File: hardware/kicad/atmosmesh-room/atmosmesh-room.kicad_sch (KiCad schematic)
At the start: 38 parts, among them U1 IDEASPARK_ESP32_1V14_TFT_30PIN

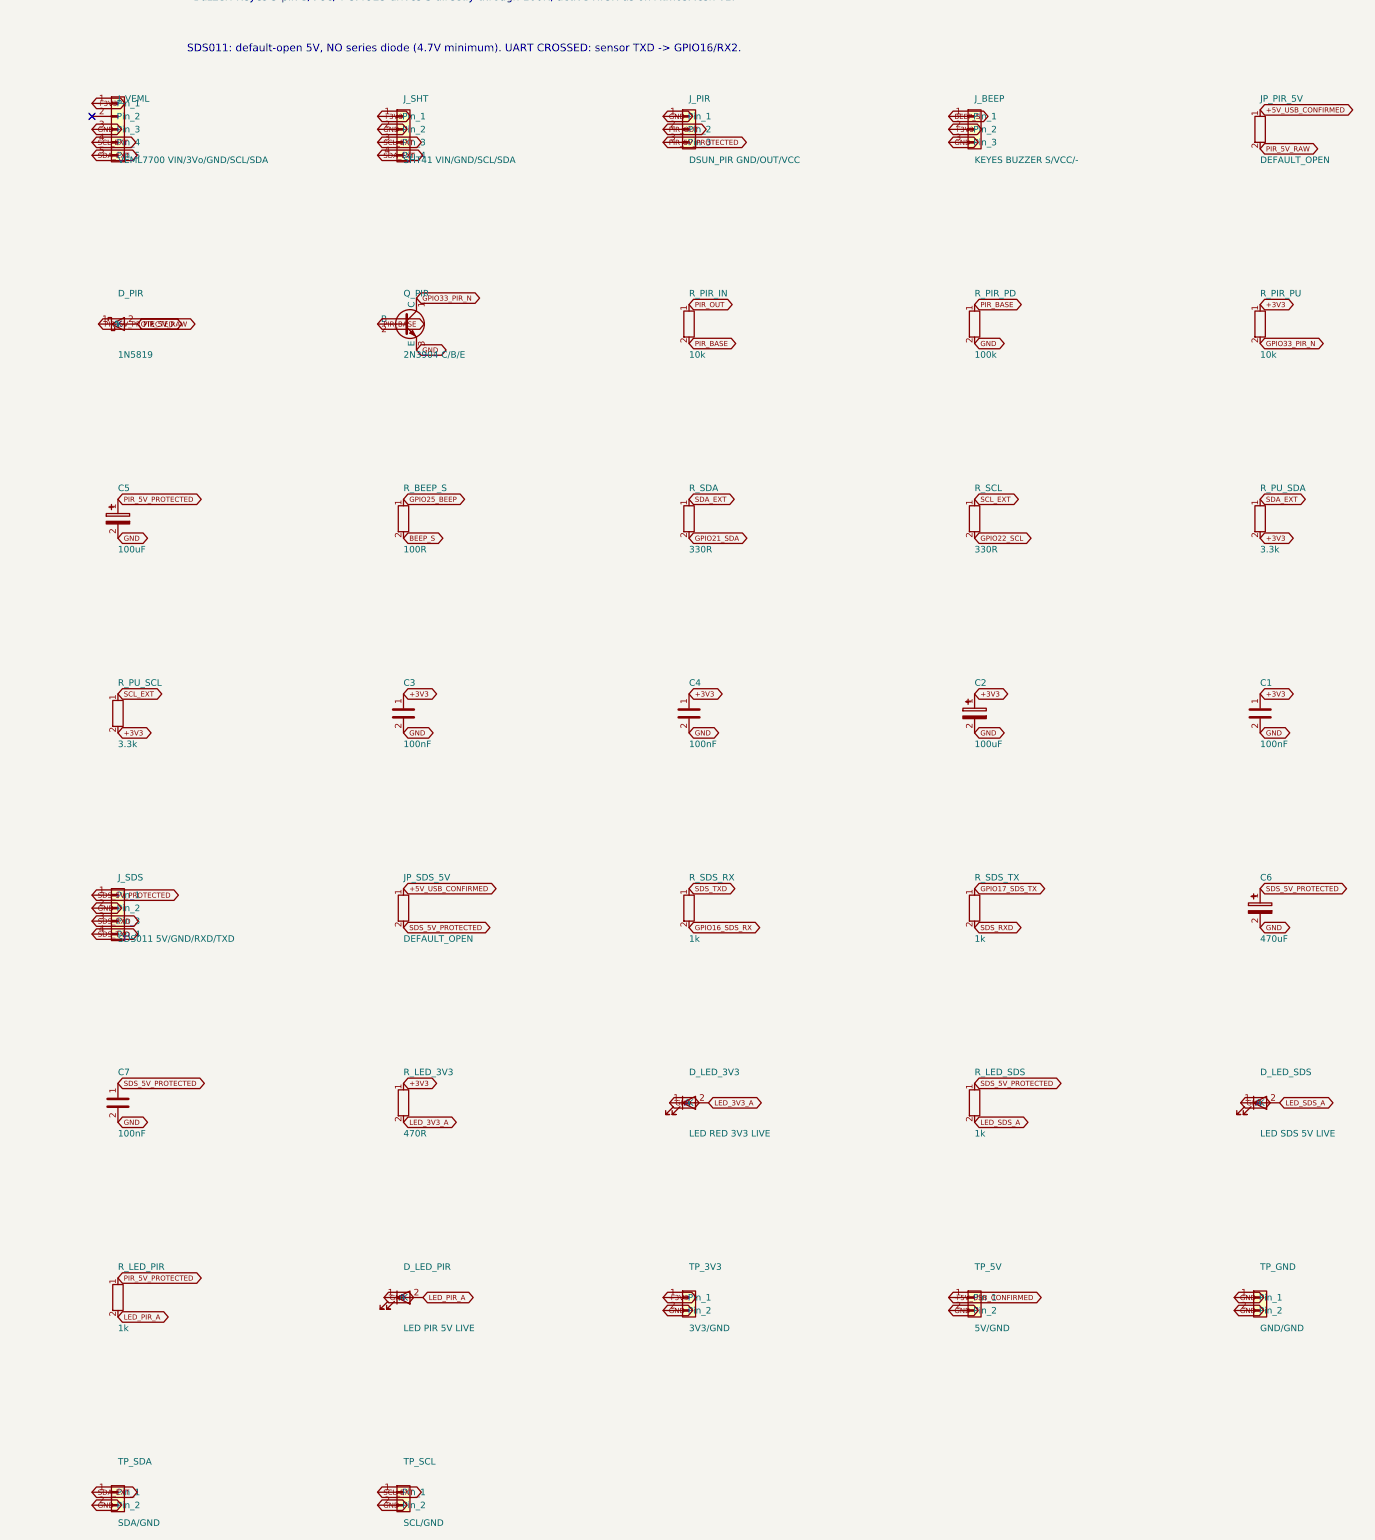
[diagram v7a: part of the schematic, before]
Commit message: :sparkles: feat(room): let the 5 V domain come from the bench supply instead of USB
The operator has a lab supply with adjustable voltage and current limit. That
changes the board, not just the procedure.

JP_5V_SRC is a 3-pin select feeding a new +5V_DOMAIN rail: shunt on 1-2 takes
the board's VIN, on 2-3 takes +5V_EXT from J_5V_EXT. JP_PIR_5V and JP_SDS_5V now
feed from +5V_DOMAIN rather than straight off VIN.

A 3-pin header accepts exactly one 2-pin shunt, so the two sources cannot be
bridged. Two independent 2-pin jumpers could both be closed and push the bench
supply back into the host's USB port. The generator refuses that arrangement and
refuses a domain wired straight to VIN; both mutation-proved.

This resolves an open blocker rather than measuring around it. spec-comparison.md
puts the USB rail near 650 mA peak coincidence before the SDS011 fan is added and
says 700 mA is not comfortable. With the external source selected the fan is not
on that rail at all.

Bring-up rule recorded in D-031: first power-up uses the external supply with the
current limit set just above the expected draw. A current-limited supply turns a
wiring error from a destroyed part into a supply that refuses to deliver - the
cheapest protection available to a project that has already lost an LDO once.

Also fixes a latent generator bug found on the way: silkscreen-vs-drawing layer
was chosen by a hard-coded index set, so every text inserted above position 8
silently moved a different label onto silkscreen. Layer is now stated per entry.

Gates: ERC 0, DRC 0 violations and 0 parity problems, both validators PASS,
git diff --check clean.
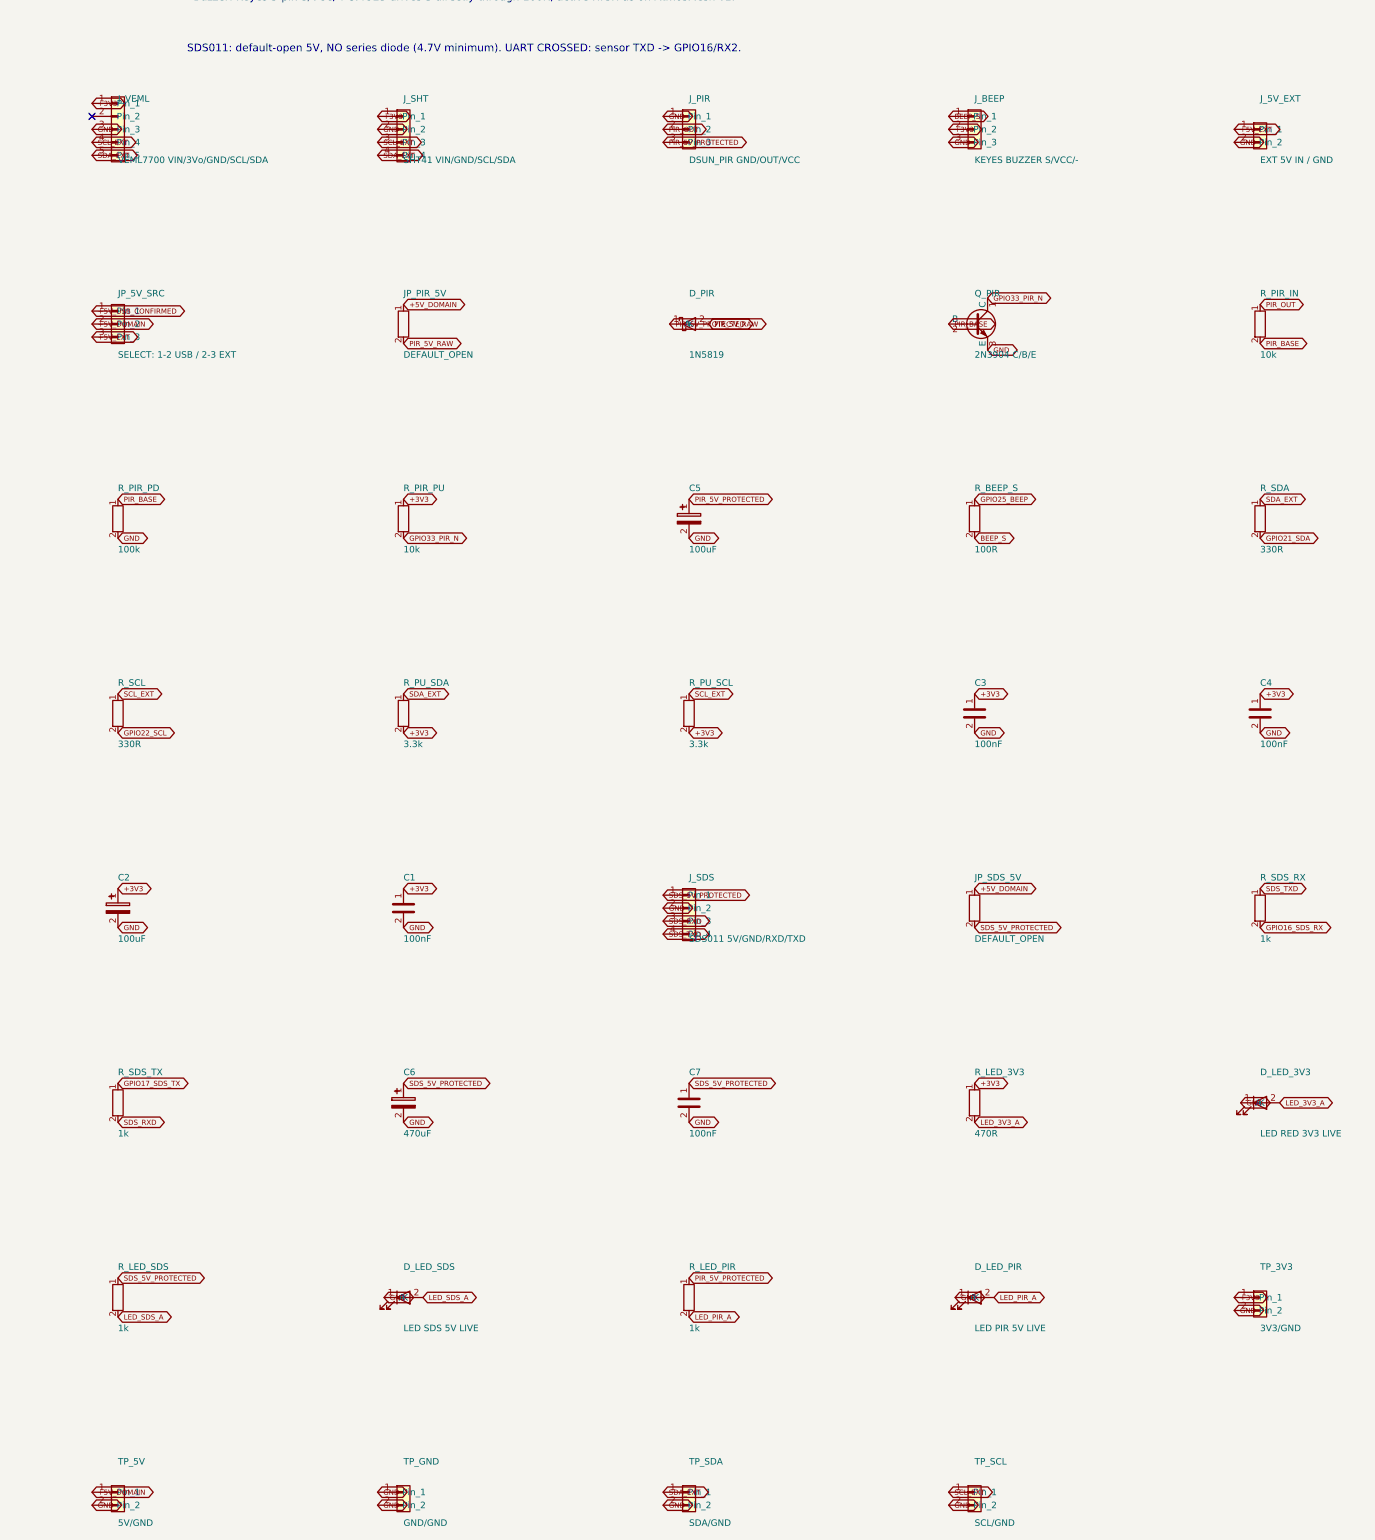
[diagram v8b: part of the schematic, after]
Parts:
- added JP_5V_SRC: SELECT: 1-2 USB / 2-3 EXT, room:PinHeader_1x03_P2.54mm, symbol atmosmesh:Conn_01x03
- added J_5V_EXT: EXT 5V IN / GND, room:PinHeader_1x02_P2.54mm, symbol atmosmesh:Conn_01x02
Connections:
- net +5V_USB_CONFIRMED: now also JP_5V_SRC.1 (Pin_1); no longer JP_PIR_5V.1, JP_SDS_5V.1, TP_5V.1 (Pin_1)
- net GND: now also J_5V_EXT.2 (Pin_2)
- new net +5V_DOMAIN: JP_5V_SRC.2 (Pin_2), JP_PIR_5V.1, JP_SDS_5V.1, TP_5V.1 (Pin_1)
- new net +5V_EXT: JP_5V_SRC.3 (Pin_3), J_5V_EXT.1 (Pin_1)
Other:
- moved on the sheet: C1, C2, C3, C4, C5, C6, C7, D_LED_3V3, D_LED_PIR, D_LED_SDS, D_PIR, JP_PIR_5V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
